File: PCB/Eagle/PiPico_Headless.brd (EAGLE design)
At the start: 67.3 x 53 mm, 14 parts, among them U1 RASPBERRY_PICOTH, X1 TOBU3, X2 TOBU3, X3 TOBU3

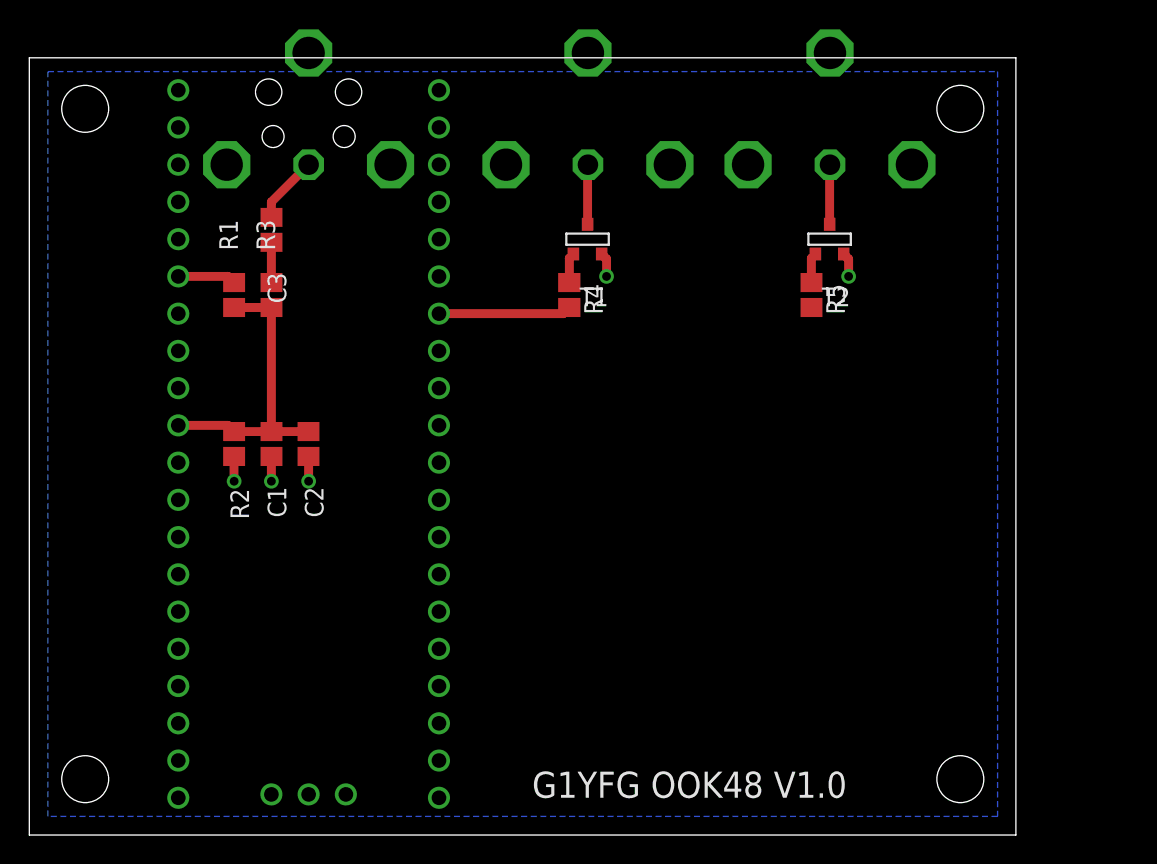
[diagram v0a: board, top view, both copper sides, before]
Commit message: Fixed a FIFO race condition
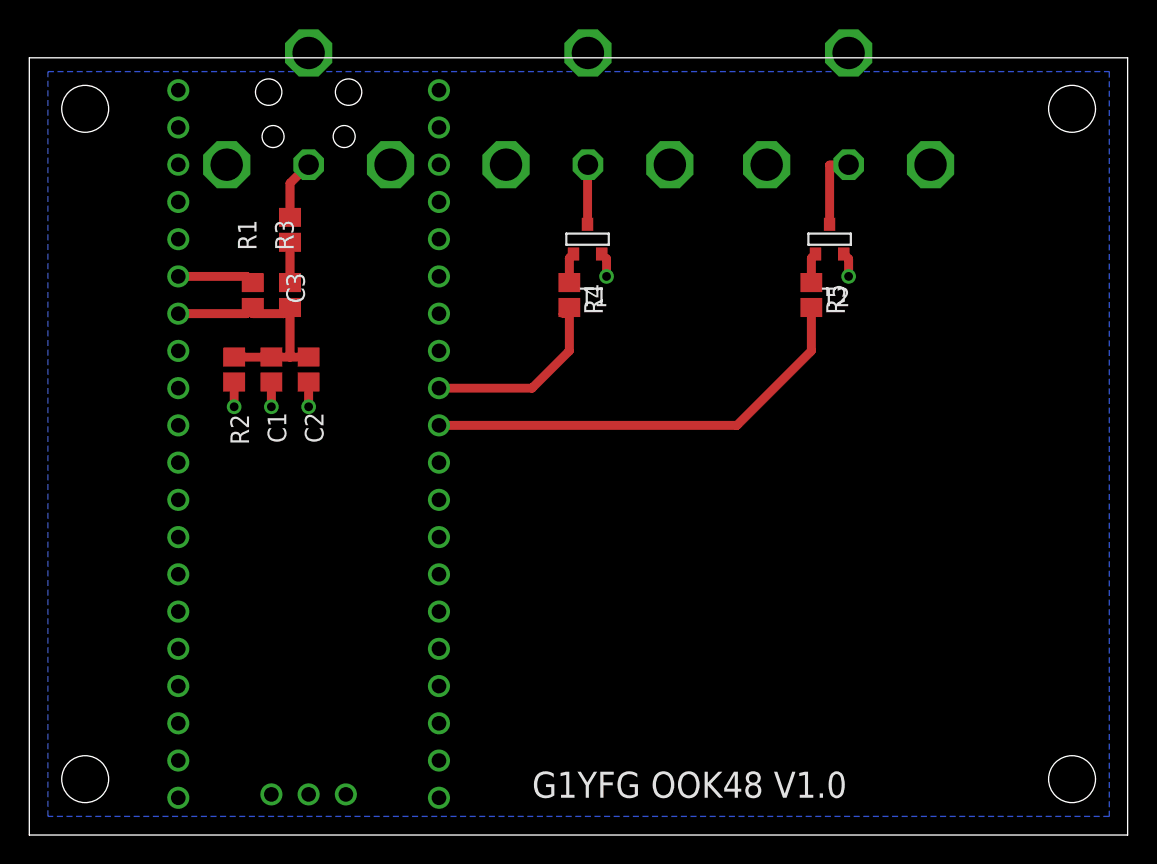
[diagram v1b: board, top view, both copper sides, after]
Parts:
- X1: value TOBU3 -> AUDIO_IN
- X2: value TOBU3 -> TX_OUT
- X3: value TOBU3 -> KEY_OUT
- moved C1 5.08 mm to (11.4, 31.8)
- moved C2 5.08 mm to (14.0, 31.8)
- moved R2 5.08 mm to (8.89, 31.8)
- moved C3 1.27 mm to (12.7, 41.3)
- moved R1 1.27 mm to (10.2, 36.8)
- moved R3 1.27 mm to (12.7, 36.8)
- moved X3 1.27 mm to (50.8, 48.3)
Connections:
- removed net N$10: U1.9
- new net 1_PPS: U1.5
- new net GPS_RX: U1.7
- new net GP_TX: U1.6
- net GPIO_KEY: now also U1.10
- net GPIO_TX: now also U1.9; no longer U1.7
- net N$1: now also U1.34; no longer U1.31
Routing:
- net GPIO_KEY: track 0.00 -> 30.5 mm
- net GPIO_TX: track 9.06 -> 13.5 mm
- net N$1: track 20.1 -> 16.8 mm
- net N$4: track 3.98 -> 5.25 mm
- net N$9: track 4.07 -> 5.33 mm
- net N$6: track 4.65 -> 4.12 mm
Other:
- board size 67.3 x 53 mm -> 74.9 x 53 mm

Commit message: V1.0 PCB
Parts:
- added C4, C5: 100nF, resistor:C0805
- added U$1: GPS, gps:GPS
- moved T1 3.81 mm to (33.0, 36.8)
- moved R4 3.81 mm to (31.8, 33.0)
- moved C3 3.59 mm to (15.2, 38.7)
- moved R5 2.84 mm to (49.5, 34.3)
- moved T2 2.84 mm to (50.8, 38.1)
- moved X1 2.54 mm to (14.0, 45.7)
- moved X2 2.54 mm to (33.0, 45.7)
- moved X3 2.54 mm to (50.8, 45.7)
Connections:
- removed net 3V3(OUT): U1.36
- removed net GP_TX: U1.6
- new net 3V3: U$1.P$5, U1.36
- new net GPS_TX: U$1.P$2, U1.6
- net 1_PPS: now also U$1.P$1
- net GND: now also C4.1, C5.1, U$1.P$4
- net GPS_RX: now also U$1.P$3
- net N$8: now also C4.2
- net N$9: now also C5.2
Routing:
- net 3V3: track 0.00 -> 49.9 mm, vias 0 -> 1
- net GPS_TX: track 0.00 -> 26.5 mm
- net GPS_RX: track 0.00 -> 26.5 mm
- net 1_PPS: track 0.00 -> 26.5 mm
- net N$8: track 4.07 -> 10.0 mm
- net GPIO_TX: track 13.5 -> 9.48 mm
- net GND: track 8.39 -> 11.8 mm, vias 5 -> 7
- net N$9: track 5.33 -> 8.32 mm
- net GPIO_KEY: track 30.5 -> 28.8 mm

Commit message: Updated PCB
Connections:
- net GPS_RX: now also U$1.P$2; no longer U$1.P$3
- net GPS_TX: now also U$1.P$3; no longer U$1.P$2
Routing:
- net GPS_TX: track 26.5 -> 33.3 mm, vias 0 -> 1
- net GPS_RX: track 26.5 -> 23.2 mm
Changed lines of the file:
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@@
 <via x="36.83" y="33.02" extent="1-16" drill="0.6" shape="square"/>
 <via x="54.61" y="34.29" extent="1-16" drill="0.6" shape="square"/>
-<wire x1="13.97" y1="50.8" x2="8.382" y2="43.18" width="0" layer="19" extent="1-1"/>
 <wire x1="36.83" y1="33.02" x2="36.83" y2="34.71" width="0.4064" layer="1"/>
 <wire x1="54.61" y1="34.29" x2="54.61" y2="35.98" width="0.4064" layer="1"/>
+<wire x1="8.382" y1="43.18" x2="13.97" y2="50.8" width="0" layer="19" extent="1-1"/>
 </signal>
 <signal name="N$3">
@@
 <signal name="GPS_RX">
 <contactref element="U1" pad="7"/>
-<contactref element="U$1" pad="P$3"/>
 <wire x1="22.86" y1="35.56" x2="25.4" y2="35.56" width="0.4064" layer="16"/>
 <wire x1="25.4" y1="35.56" x2="26.67" y2="34.29" width="0.4064" layer="16"/>
-<wire x1="26.67" y1="34.29" x2="26.67" y2="19.05" width="0.4064" layer="16"/>
-<wire x1="26.67" y1="19.05" x2="27.94" y2="17.78" width="0.4064" layer="16"/>
-<wire x1="27.94" y1="17.78" x2="33.02" y2="17.78" width="0.4064" layer="16"/>
+<contactref element="U$1" pad="P$2"/>
+<wire x1="26.67" y1="34.29" x2="26.67" y2="22.86" width="0.4064" layer="16"/>
+<wire x1="26.67" y1="22.86" x2="29.21" y2="20.32" width="0.4064" layer="16"/>
+<wire x1="29.21" y1="20.32" x2="33.02" y2="20.32" width="0.4064" layer="16"/>
 </signal>
 <signal name="1_PPS">
@@
 </signal>
 <signal name="GPS_TX">
-<contactref element="U$1" pad="P$2"/>
 <contactref element="U1" pad="6"/>
 <wire x1="22.86" y1="38.1" x2="26.67" y2="38.1" width="0.4064" layer="16"/>
 <wire x1="26.67" y1="38.1" x2="27.94" y2="36.83" width="0.4064" layer="16"/>
-<wire x1="27.94" y1="36.83" x2="27.94" y2="21.59" width="0.4064" layer="16"/>
-<wire x1="27.94" y1="21.59" x2="29.21" y2="20.32" width="0.4064" layer="16"/>
-<wire x1="29.21" y1="20.32" x2="33.02" y2="20.32" width="0.4064" layer="16"/>
+<contactref element="U$1" pad="P$3"/>
+<wire x1="27.94" y1="36.83" x2="27.94" y2="25.4" width="0.4064" layer="16"/>
+<via x="27.94" y="25.4" extent="1-16" drill="0.6"/>
+<wire x1="27.94" y1="25.4" x2="34.29" y2="25.4" width="0.4064" layer="1"/>
+<wire x1="34.29" y1="25.4" x2="35.56" y2="24.13" width="0.4064" layer="1"/>
+<wire x1="35.56" y1="24.13" x2="35.56" y2="19.05" width="0.4064" layer="1"/>
+<wire x1="35.56" y1="19.05" x2="34.29" y2="17.78" width="0.4064" layer="1"/>
+<wire x1="34.29" y1="17.78" x2="33.02" y2="17.78" width="0.4064" layer="1"/>
 </signal>
 <signal name="3V3">
@@
 <wire x1="33.02" y1="12.7" x2="30.48" y2="12.7" width="0.4064" layer="1"/>
 <wire x1="30.48" y1="12.7" x2="29.21" y2="13.97" width="0.4064" layer="1"/>
-<wire x1="29.21" y1="13.97" x2="29.21" y2="22.86" width="0.4064" layer="1"/>
-<wire x1="29.21" y1="22.86" x2="27.94" y2="24.13" width="0.4064" layer="1"/>
-<wire x1="27.94" y1="24.13" x2="20.32" y2="24.13" width="0.4064" layer="1"/>
-<wire x1="20.32" y1="24.13" x2="19.05" y2="25.4" width="0.4064" layer="1"/>
-<wire x1="19.05" y1="25.4" x2="19.05" y2="34.29" width="0.4064" layer="1"/>
+<wire x1="29.21" y1="13.97" x2="29.21" y2="20.32" width="0.4064" layer="1"/>
+<wire x1="29.21" y1="20.32" x2="27.94" y2="21.59" width="0.4064" layer="1"/>
+<wire x1="27.94" y1="21.59" x2="20.32" y2="21.59" width="0.4064" layer="1"/>
+<wire x1="20.32" y1="21.59" x2="19.05" y2="22.86" width="0.4064" layer="1"/>
+<wire x1="19.05" y1="22.86" x2="19.05" y2="34.29" width="0.4064" layer="1"/>
 <wire x1="19.05" y1="34.29" x2="17.78" y2="35.56" width="0.4064" layer="1"/>
 <via x="17.78" y="35.56" extent="1-16" drill="0.6" shape="square"/>
